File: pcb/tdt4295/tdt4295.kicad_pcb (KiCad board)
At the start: 6 copper layers, 169 parts, among them J101 ARM 20 Pin Debug Header, J102 MCU USART1 Header, J103 DM1AA-SF-PEJ(21), J104 MCU GPIO Header, J301 FPGA__debug, J501 618015330923, J502 FPGA GPIO, P201 690-005-299-043, U101 EFM32GG12B810F1024GQ64, U102 COM-09032 Joystick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

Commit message: wrap up today's shift in the coal mines
:')
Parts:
- C101, C102, C103, C104, C105, C106, C107, C108, C109, C110, C111: moved to B.Cu
- moved J103 109.2 mm to (303.2, 31.1)
- moved R105 92.1 mm to (282.1, 64.1), turned to 180 degrees
- moved R106 91.8 mm to (282.1, 69.8), turned to 180 degrees
- moved D101 85.3 mm to (167.6, 103.5), turned to 90 degrees
- moved D102 82.8 mm to (173.4, 103.5), turned to 90 degrees
- moved D103 80.8 mm to (179.1, 103.5), turned to 90 degrees
- moved R101 79.9 mm to (167.6, 111.2), turned to 270 degrees
- moved D104 79.4 mm to (184.8, 103.5), turned to 90 degrees
- moved R102 73.8 mm to (173.4, 111.3), turned to 270 degrees
- moved R103 68.2 mm to (179.1, 111.3), turned to 270 degrees
- moved R104 63.3 mm to (184.8, 111.3), turned to 270 degrees
- moved J102 58.5 mm to (232.4, 20.3), turned to 90 degrees
- moved R110 50.8 mm to (148.6, 103.5)
- moved R111 46.5 mm to (152.4, 103.5)
- moved R113 37.8 mm to (160.0, 103.5)
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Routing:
- net +3V3: track 150.0 -> 425.0 mm, vias 33 -> 50
- net GND: track 255.5 -> 416.6 mm, vias 150 -> 173
- net GPIO_BTN0: track 0.00 -> 149.1 mm, vias 0 -> 1
- net USART1_CLK: track 0.00 -> 126.0 mm, vias 0 -> 2
- net USART1_CS: track 0.00 -> 125.5 mm, vias 0 -> 2
- net USART1_TX: track 0.00 -> 123.7 mm, vias 0 -> 2
- net USART1_CTS: track 0.00 -> 122.4 mm, vias 0 -> 2
- net USART1_RX: track 0.00 -> 118.2 mm, vias 0 -> 2
- net GPIO_BTN1: track 0.00 -> 107.9 mm, vias 0 -> 1
- net +1V0: track 130.2 -> 214.1 mm
- net +1V8: track 120.5 -> 194.2 mm, vias 11 -> 12
- net GPIO_BTN3: track 0.00 -> 67.9 mm
- net FPGA_MCU_GPIO_3: track 17.3 -> 83.6 mm
- net FPGA_MCU_GPIO_2: track 18.3 -> 84.3 mm
- net GPIO_BTN2: track 0.00 -> 62.7 mm
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
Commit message: The fight is almost over!
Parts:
- added G***: LOGO, Graphics:buggelogo_43mm, F.Cu at (183.4, 49.0)
- U301: value S25FL127SABMFV101 -> SOC008_SPA
- moved TP201 146.8 mm to (234.8, 52.3), turned to 180 degrees
- moved TP202 145.6 mm to (224.8, 52.3), turned to 180 degrees
- moved TP205 140.3 mm to (264.8, 52.3), turned to 180 degrees
- moved TP203 137.9 mm to (244.8, 52.3), turned to 180 degrees
- moved TP204 137.1 mm to (254.8, 52.3), turned to 180 degrees
- moved U502 85.5 mm to (108.7, 34.5)
- moved U501 84.7 mm to (140.3, 34.5)
- moved U503 84.1 mm to (108.7, 27.9)
- moved J502 83.7 mm to (123.8, 29.7)
- moved U504 83.4 mm to (140.3, 27.9)
- moved R305 74.1 mm to (146.6, 77.5), turned to 90 degrees
- moved R507 73.2 mm to (133.6, 100.3)
- moved R508 72.7 mm to (140.2, 100.3)
- moved R509 72.7 mm to (147.3, 100.3)
- moved R510 72.6 mm to (154.4, 100.3)
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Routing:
- net GPIO_BTN0: track 149.1 -> 34.6 mm, vias 1 -> 2
- net USART1_CTS: track 122.4 -> 30.1 mm
- net USART1_CS: track 125.5 -> 35.2 mm
- net USART1_CLK: track 126.0 -> 39.4 mm
- net +1V0: track 214.1 -> 129.0 mm, vias 26 -> 29
- net +1V8: track 194.2 -> 278.0 mm, vias 12 -> 13
- net USART1_TX: track 123.7 -> 45.3 mm
- net USART1_RX: track 118.2 -> 42.3 mm
- net GPIO_BTN1: track 107.9 -> 34.5 mm, vias 1 -> 2
- net Net-(J501-Pad2): track 0.00 -> 65.6 mm
- net FPGA_EXT_IO5: track 15.8 -> 75.4 mm, vias 0 -> 2
- net Net-(J501-Pad1): track 0.00 -> 58.5 mm
- net VGA_VS: track 7.58 -> 65.6 mm, vias 1 -> 2
- net FPGA_EXT_IO4: track 15.9 -> 71.8 mm, vias 0 -> 2
- net FPGA_LED1: track 4.09 -> 59.8 mm, vias 0 -> 2
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- added copper zone on +PWR, net +5V
- added copper zone on In3.Cu, net Net-(C501-Pad2)

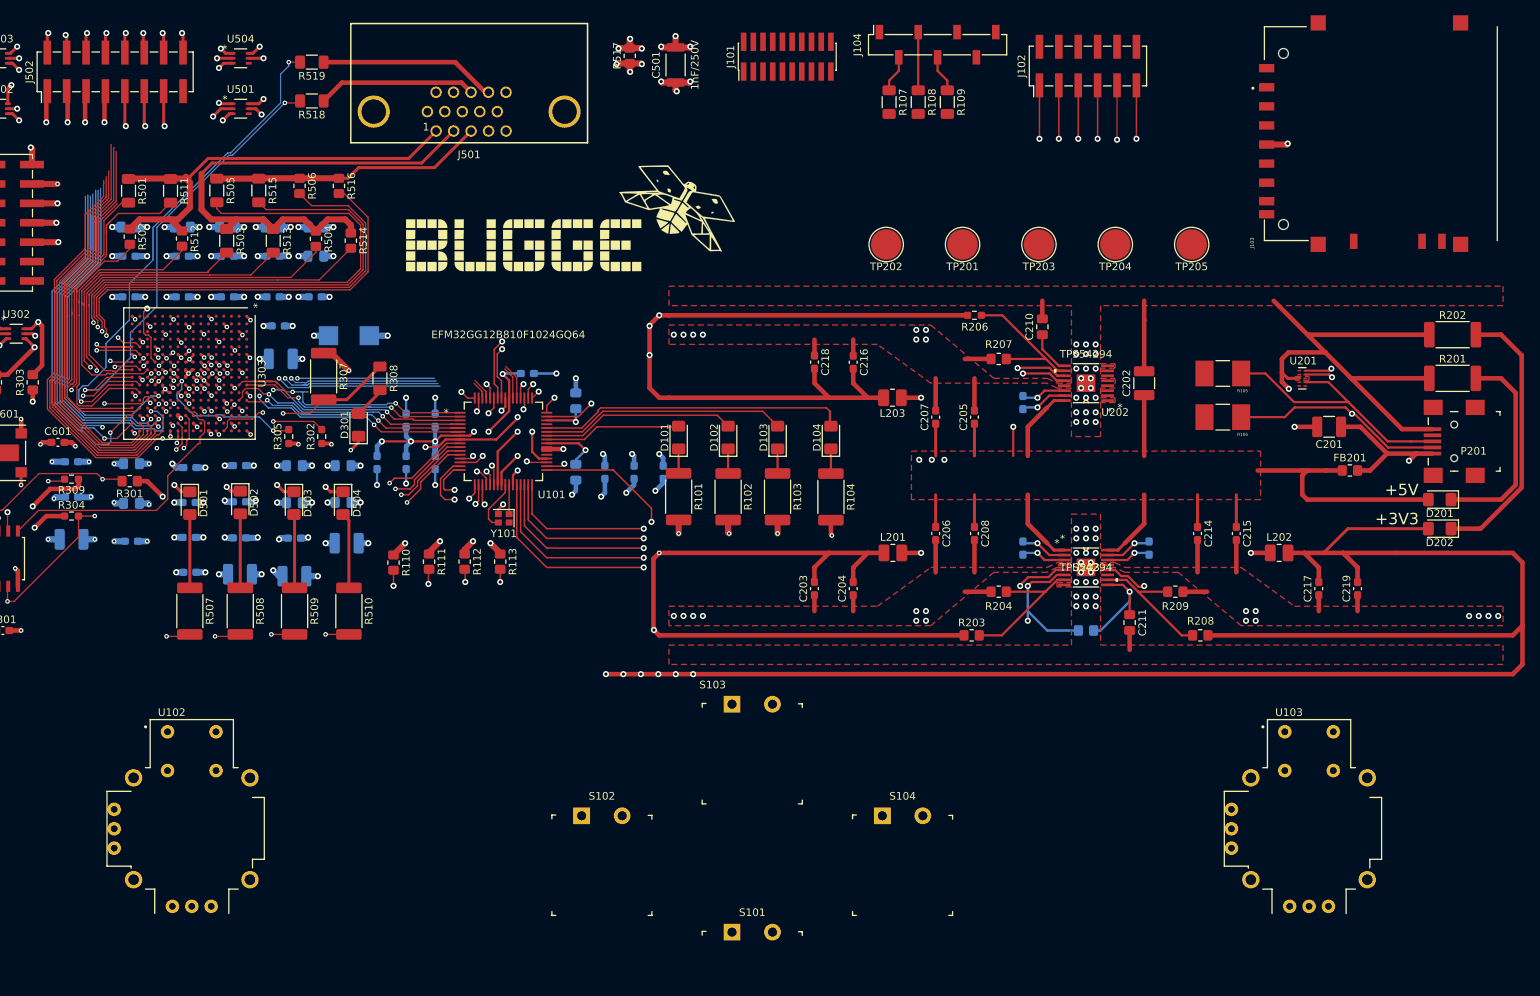
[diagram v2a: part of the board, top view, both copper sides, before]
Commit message: make longest connections
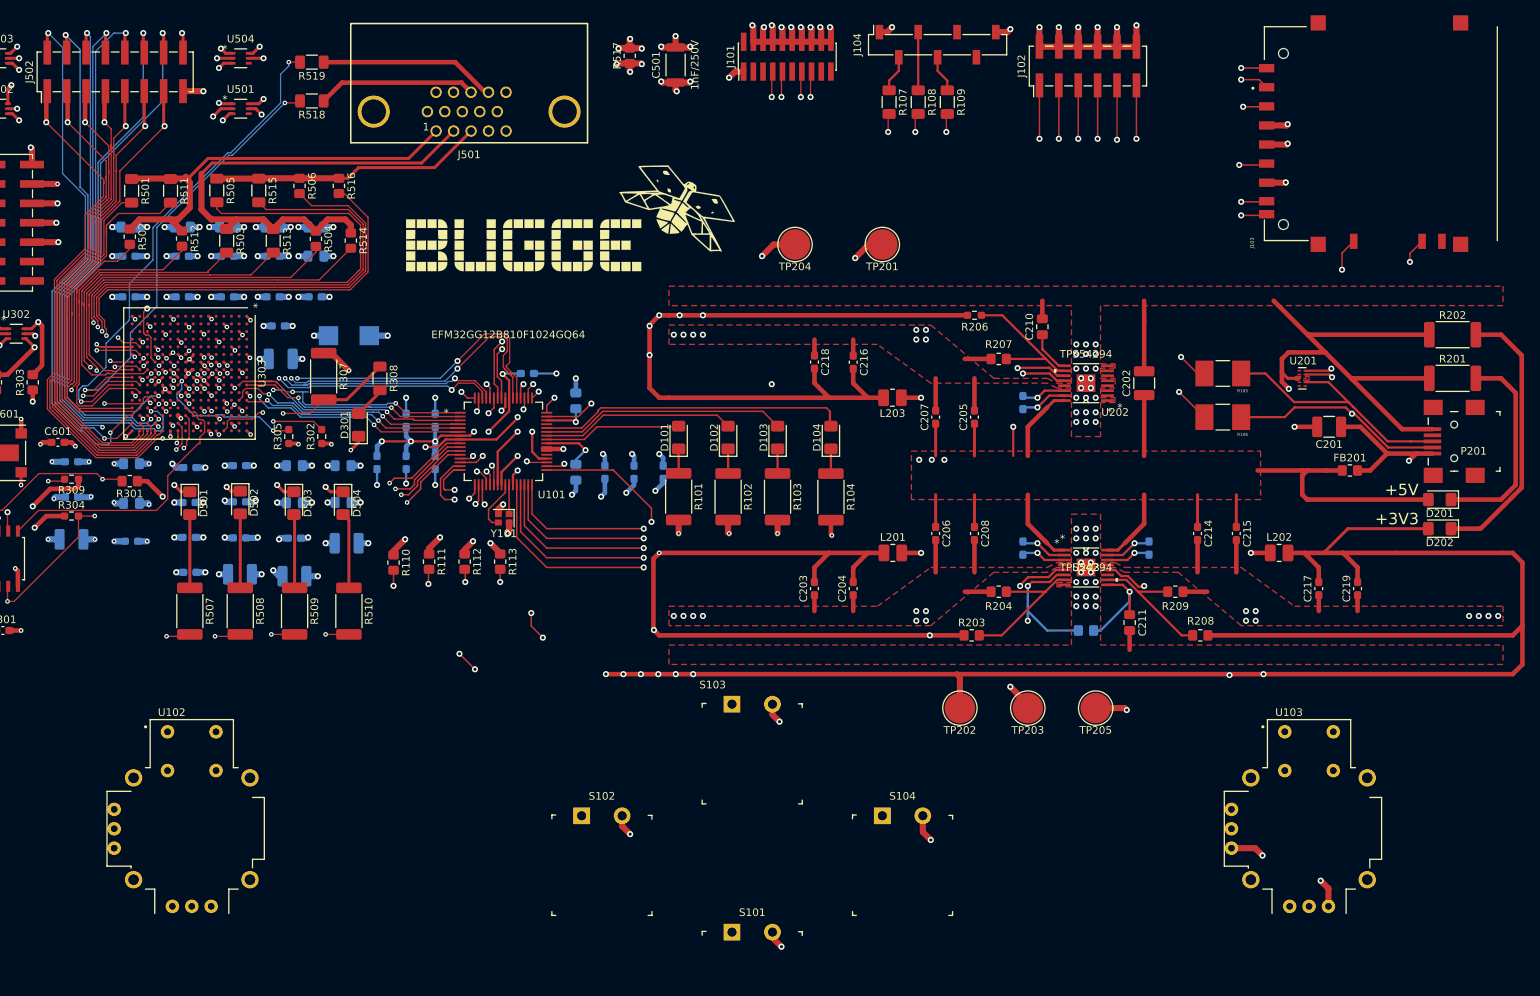
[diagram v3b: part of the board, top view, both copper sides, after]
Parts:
- moved TP205 62.0 mm to (252.2, 113.0)
- moved TP202 61.5 mm to (234.4, 113.0)
- moved TP203 60.7 mm to (243.3, 113.0)
- moved TP204 41.9 mm to (212.9, 52.3)
- moved TP201 10.5 mm to (224.3, 52.3)
- moved R501 0.41 mm to (126.0, 45.3)
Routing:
- net SDIO_WP: track 23.0 -> 145.3 mm, vias 1 -> 2
- net SDIO_CD: track 20.8 -> 134.6 mm, vias 1 -> 2
- net GPIO_JSH1: track 25.1 -> 137.9 mm
- net SDIO_DAT2: track 13.1 -> 123.0 mm, vias 1 -> 2
- net SDIO_DAT3: track 12.8 -> 122.5 mm, vias 1 -> 2
- net SDIO_CMD: track 17.0 -> 124.9 mm, vias 1 -> 2
- net SDIO_CLK: track 19.1 -> 124.0 mm, vias 1 -> 2
- net SDIO_DAT0: track 13.2 -> 116.3 mm, vias 1 -> 2
- net SDIO_DAT1: track 15.8 -> 118.2 mm, vias 1 -> 2
- net GPIO_JSV1: track 18.3 -> 116.1 mm
- net GND: track 438.3 -> 531.3 mm, vias 197 -> 224
- net Net-(R106-Pad2): track 6.55 -> 92.0 mm, vias 1 -> 2
- net USART1_CTS: track 30.1 -> 114.7 mm
- net Net-(R105-Pad2): track 11.8 -> 92.5 mm, vias 1 -> 2
- net USART1_RTS: track 27.0 -> 107.7 mm
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
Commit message: tidy up routing a little bit
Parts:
- moved TP203 94.3 mm to (149.9, 100.3)
- moved TP205 85.4 mm to (190.5, 54.0)
- moved TP204 66.3 mm to (149.9, 73.0)
- moved TP201 59.5 mm to (175.9, 87.0)
- moved G*** 52.6 mm to (130.8, 48.9)
- moved J102 49.5 mm to (201.9, 33.4)
- moved D201 49.1 mm to (248.4, 90.2)
- moved D202 49.1 mm to (248.4, 94.0)
- moved R201 49.1 mm to (250.1, 74.3)
- moved R202 49.1 mm to (250.1, 68.6)
- moved R208 49.1 mm to (217.0, 108.0)
- moved U201 49.1 mm to (230.4, 74.3)
- moved C101 49.1 mm to (109.2, 85.3)
- moved C102 49.1 mm to (113.0, 85.3)
- moved C103 49.1 mm to (113.0, 79.8)
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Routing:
- net +3V3: track 449.3 -> 848.7 mm, vias 76 -> 71
- net +1V8: track 294.8 -> 211.6 mm, vias 15 -> 12
- net GND: track 531.3 -> 471.5 mm, vias 224 -> 204
- net +5V: track 131.7 -> 179.9 mm, vias 8 -> 6
- net Net-(U103-PadS1): track 0.00 -> 41.9 mm
- net Net-(U102-PadS1): track 0.00 -> 41.9 mm
- net Net-(C501-Pad2): track 9.70 -> 51.4 mm, vias 6 -> 3
- net USART1_TX: track 114.0 -> 151.8 mm
- net USART1_RX: track 113.6 -> 148.1 mm
- net USART1_CLK: track 113.2 -> 144.5 mm
- net +1V0: track 150.6 -> 181.9 mm, vias 32 -> 27
- net USART1_CS: track 111.6 -> 140.8 mm
- net USART1_RTS: track 107.7 -> 130.2 mm
- net USART1_CTS: track 114.7 -> 135.9 mm
- net Net-(P201-PadSH): track 0.00 -> 19.9 mm
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- removed copper zone on +PWR, net +5V
- removed copper zone on In3.Cu, net Net-(C501-Pad2)
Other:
- board outline added: 209.6 x 139.7 mm
- board text added: "+1V0"
- board text added: "+1V8"
- board text added: "Eirik Wittersø Embla Flatlandsmo Erling Feet Nesset Jørgen Aleksander Fagervik"
- board text added: "GND"
- board text added: "Karoline Kanestrøm Sæbø Ole Ludvig Hozman Markus Wang Halvorsen Steffen André Haug"
- board text added: "RDY"
